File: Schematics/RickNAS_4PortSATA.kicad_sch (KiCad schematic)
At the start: 9 parts, among them U1 SATA_Combined, U2 SATA_Data, U3 SATA_Power, U4 SATA_Combined, U5 SATA_Data, U6 SATA_Combined, U7 SATA_Data, U8 SATA_Combined, U9 SATA_Data

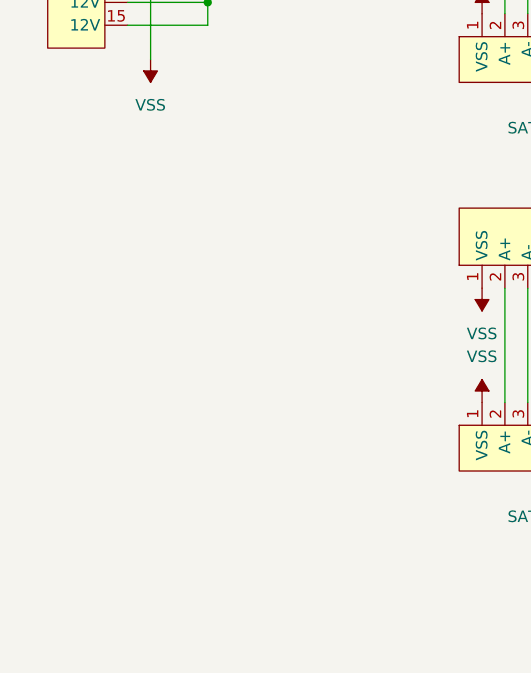
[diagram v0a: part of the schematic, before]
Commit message: Assigned some footprints. Where is that sata power part?
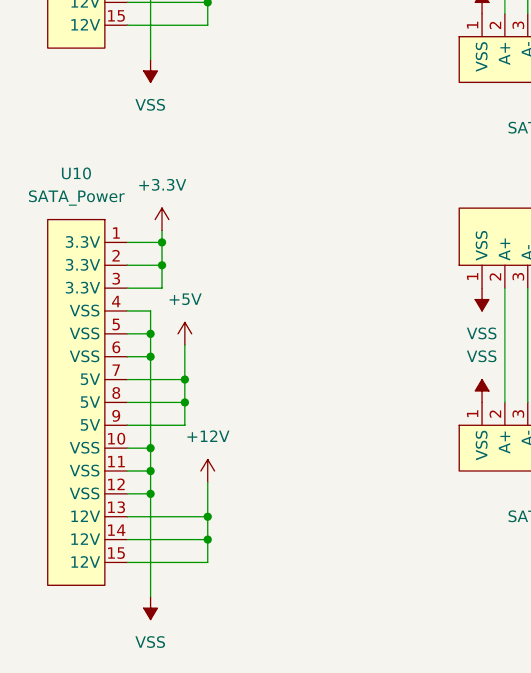
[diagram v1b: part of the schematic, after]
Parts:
- added U10: SATA_Power, symbol UE-Connector:SATA_Power-15Pin
- U1, U4, U6, U8: footprint (none) -> UE-Connector:CONN22_1735284-3_TEC
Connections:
- net +12V: now also U10.13 (12V), U10.14 (12V), U10.15 (12V)
- net +3.3V: now also U10.1 (3.3V), U10.2 (3.3V), U10.3 (3.3V)
- net +5V: now also U10.7 (5V), U10.8 (5V), U10.9 (5V)
- net VSS: now also U10.10 (VSS), U10.11 (VSS), U10.12 (VSS), U10.4 (VSS), U10.5 (VSS), U10.6 (VSS)

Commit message: Ordering PCBs
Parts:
- U1, U4, U6, U8: footprint UE-Connector:CONN22_1735284-3_TEC -> UE-Connector:CONN22_877811_MOL
- U10, U3: footprint (none) -> UE-Connector:alim_SATA
- U2, U5, U7, U9: footprint (none) -> UE-Connector:CONN_67490-1220_MOL
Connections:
- net +12V: no longer U10.13 (12V), U10.14 (12V), U10.15 (12V), U4.20 (12V), U4.21 (12V), U4.22 (12V), U8.20 (12V), U8.21 (12V), U8.22 (12V)
- net +3.3V: no longer U10.1 (3.3V), U10.2 (3.3V), U10.3 (3.3V), U4.10 (3.3V), U4.8 (3.3V), U4.9 (3.3V), U8.10 (3.3V), U8.8 (3.3V), U8.9 (3.3V)
- net +5V: no longer U10.7 (5V), U10.8 (5V), U10.9 (5V), U4.14 (5V), U4.15 (5V), U4.16 (5V), U8.14 (5V), U8.15 (5V), U8.16 (5V)
- net A1+: now reaches U4.2 (A+), U5.2 (A+)
- net A1-: now reaches U4.3 (A-), U5.3 (A-)
- net B1-: now reaches U4.5 (B-), U5.5 (B-)
- net B1+: now reaches U4.6 (B+), U5.6 (B+)
- net A2+: now reaches U6.2 (A+), U7.2 (A+)
- net A2-: now reaches U6.3 (A-), U7.3 (A-)
- net B2-: now reaches U6.5 (B-), U7.5 (B-)
- net B2+: now reaches U6.6 (B+), U7.6 (B+)
- net A3+: now reaches U8.2 (A+), U9.2 (A+)
- net A3-: now reaches U8.3 (A-), U9.3 (A-)
- net B3-: now reaches U8.5 (B-), U9.5 (B-)
- net B3+: now reaches U8.6 (B+), U9.6 (B+)
- net A+: now reaches U1.2 (A+), U2.2 (A+)
- net A-: now reaches U1.3 (A-), U2.3 (A-)
- net B-: now reaches U1.5 (B-), U2.5 (B-)
- net B+: now reaches U1.6 (B+), U2.6 (B+)
- new net +12P: U10.13 (12V), U10.14 (12V), U10.15 (12V), U4.20 (12V), U4.21 (12V), U4.22 (12V), U8.20 (12V), U8.21 (12V), U8.22 (12V)
- new net +3.3VP: U10.1 (3.3V), U10.2 (3.3V), U10.3 (3.3V), U4.10 (3.3V), U4.8 (3.3V), U4.9 (3.3V), U8.10 (3.3V), U8.8 (3.3V), U8.9 (3.3V)
- new net +5P: U10.7 (5V), U10.8 (5V), U10.9 (5V), U4.14 (5V), U4.15 (5V), U4.16 (5V), U8.14 (5V), U8.15 (5V), U8.16 (5V)
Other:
- moved on the sheet: U1, U2, U4, U5, U6, U7, U8, U9

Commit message: Started CAD
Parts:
- added D1, D2, D3, D4: LED_Small, LED_SMD:LED_0805_2012Metric, symbol Device:LED_Small
- added H1, H2, H3, H4: MountingHole_Pad, MountingHole:MountingHole_3.2mm_M3_DIN965_Pad, symbol Mechanical:MountingHole_Pad
- added RN1: R_Pack04, Resistor_SMD:R_Array_Concave_4x0603, symbol Device:R_Pack04
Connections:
- net +3.3V: now also RN1.1 (R1.1), RN1.2 (R2.1), RN1.3 (R3.1), RN1.4 (R4.1)
- net VSS: now also H1.1, H2.1, H3.1, H4.1; no longer U1.19 (VSS), U4.19 (VSS), U6.19 (VSS), U8.19 (VSS)
- new net: D1.2 (A), RN1.5 (R4.2)
- new net: D2.2 (A), RN1.6 (R3.2)
- new net: D3.2 (A), RN1.7 (R2.2)
- new net: D4.2 (A), RN1.8 (R1.2)
- new net Drive 1: D1.1 (K), U1.19 (VSS)
- new net Drive 2: D2.1 (K), U6.19 (VSS)
- new net Drive 3: D3.1 (K), U4.19 (VSS)
- new net Drive 4: D4.1 (K), U8.19 (VSS)
